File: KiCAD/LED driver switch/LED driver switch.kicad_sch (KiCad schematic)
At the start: 37 parts, among them J1 3x Banana Jack, J2 USB Jack, J3 Conn_01x04_Pin, J4 TTl-RS232, J5 JST-XH Connector, J6 8P8C_Shielded, Q1 TN2124, Q2 PMOS, SW1 Door interlock, SW2 Door interlock, SW3 Door interlock, SW4 Door interlock, U2 4.096V, U8 Itsy_Bitsy_32u4

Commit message: Initial draft
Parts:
- removed SW2, SW3: Door interlock, symbol Switch:SW_Reed
- added J7: Conn_Coaxial, Custom footprints:LINX_CONBNC001, symbol Connector:Conn_Coaxial
- added N2: Bench Supply, symbol Mechanical:Housing
- D2: footprint Custom footprints:P26_DO-214AA_SMB -> Custom footprints:SMDJSeries_LTF; Manufacturer Diotec Semiconductor -> YAGEO; Part P6SMB300A -> SMDJ220CA/TR13
- F2: Part 3403.0010.11 -> 3403.0022.24
- F3: Part 3403.0019.11 -> 3403.0022.24
- Q2: footprint Package_TO_SOT_SMD:SOT-223-3_TabPin2 -> Package_TO_SOT_SMD:TO-263-2; Part DMP45H21DHE-13 -> DMP45H4D9HK3-13
- R5: value 100 -> 1; footprint Resistor_SMD:R_1206_3216Metric -> Package_TO_SOT_SMD:TO-263-2
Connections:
- net GND: now also U8.16 (Gnd), J7.2 (Ext)
- net Isense: now also J7.1 (In)
- net Power supply+: now also F3.1; no longer F3.2
- net at D3.2 (A): now also F3.2; no longer F3.1
- net Enclosure safety interlock1: no longer names the net of U8.29 (12_A11)
- net Enclosure safety interlock2: no longer names the net of U8.28 (~11)
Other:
- moved on the sheet: J3, J4, RN2

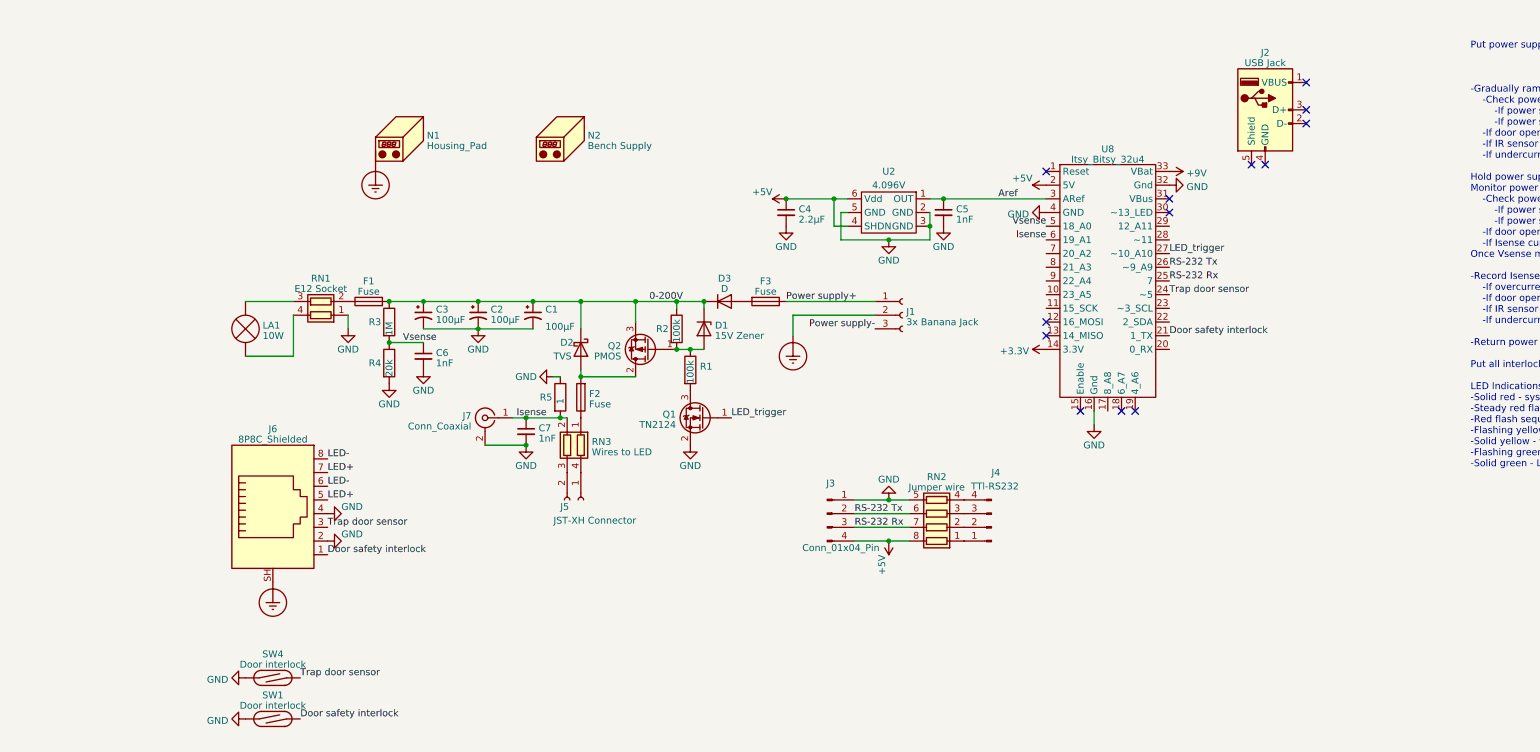
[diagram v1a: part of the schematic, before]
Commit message: Working PCB draft
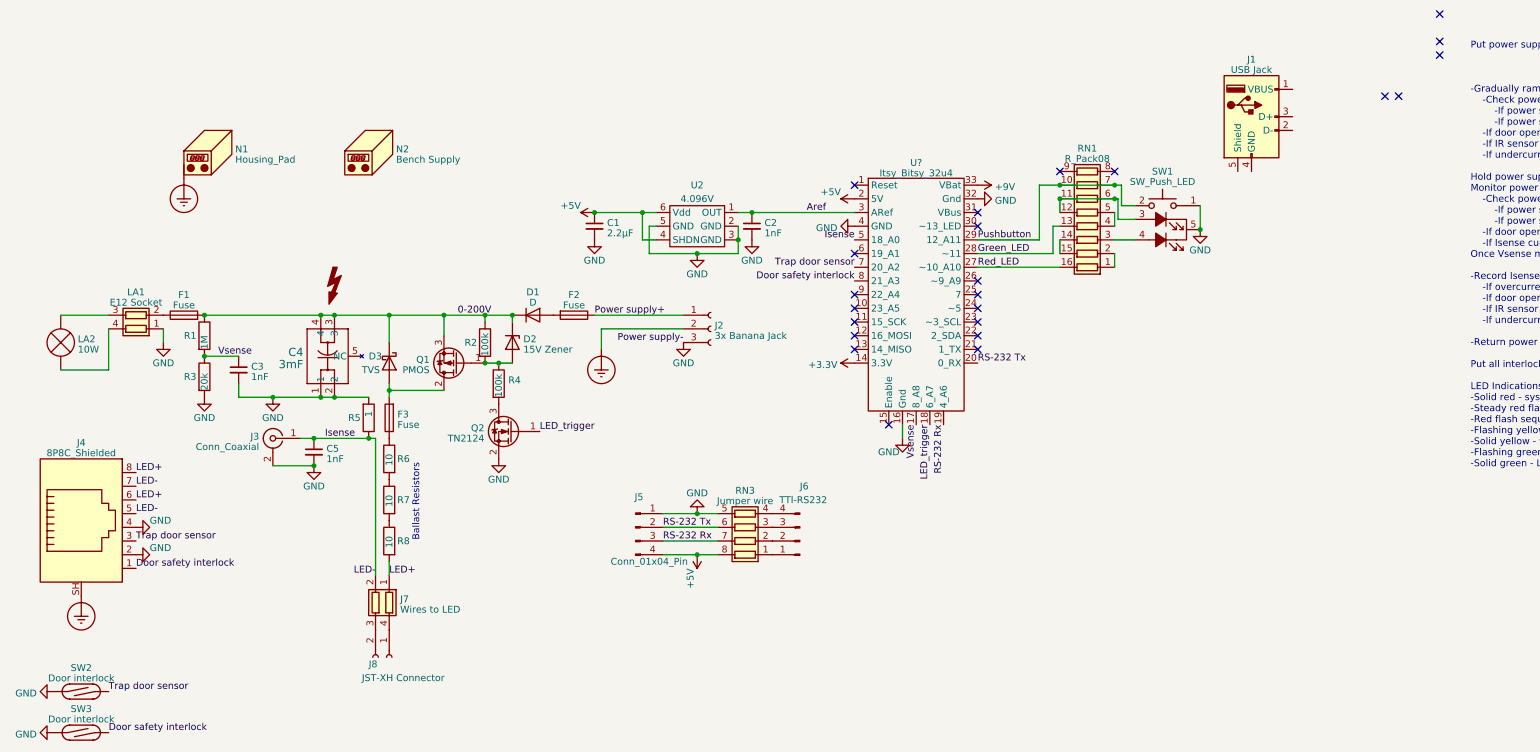
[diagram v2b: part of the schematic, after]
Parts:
- removed C1, C2, C3: 100µF, Capacitor_THT:CP_Radial_D18.0mm_P7.50mm, symbol Device:C_Polarized_Small_US
- added C4: 3mF, Custom footprints:ALF20G302KP400, symbol Custom:ALF20G223EH063
- added R6, R7, R8: 10, Package_TO_SOT_THT:TO-247-2_Vertical, symbol Device:R
- added RN1: R_Pack08, Resistor_SMD:R_Array_Convex_8x0602, symbol Device:R_Pack08
- added SW1: SW_Push_LED, Connector_Wire:SolderWire-0.1sqmm_1x05_P3.6mm_D0.4mm_OD1mm, symbol Custom:SW_Push_2x_LED_common_cathode
- added SYM1: SYM_Flash_Small, Custom footprints:Symbol_HighVoltage, symbol Graphic:SYM_Flash_Small
- J2: renamed from J1; footprint Connector_Wire:SolderWire-0.1sqmm_1x03_P3.6mm_D0.4mm_OD1mm -> Connector_Wire:SolderWire-0.15sqmm_1x03_P4mm_D0.5mm_OD1.5mm
- J3: renamed from J7; footprint Custom footprints:LINX_CONBNC001 -> Connector_Wire:SolderWire-0.1sqmm_1x02_P3.6mm_D0.4mm_OD1mm; Part CONBNC001 -> CONBNC004
- J4: renamed from J6; footprint Custom footprints:AMPHENOL_RJE3A1881402N -> Custom footprints:BEL_SS71800-019F; Manufacturer Amphenol ICC (Commercial Products) -> Stewart Connector; Part RJE3A1881402N -> SS71800-019F
- J8: renamed from J5; footprint Connector_Wire:SolderWire-0.1sqmm_1x02_P3.6mm_D0.4mm_OD1mm_Relief -> (none)
- LA1: renamed from RN1; footprint (none) -> Connector_Wire:SolderWire-0.1sqmm_1x02_P3.6mm_D0.4mm_OD1mm
- R5: footprint Package_TO_SOT_SMD:TO-263-2 -> Package_TO_SOT_THT:TO-126-2_Vertical; Manufacturer Panasonic Electronic Components -> Caddock Electronics Inc.; Part ERA-8AEB101V -> MP915-1.00-1%
- renumbered C4 to C1, C5 to C2, C6 to C3, C7 to C5, D3 to D1, D1 to D2, D2 to D3, F3 to F2, F2 to F3, J2 to J1, J3 to J5, J4 to J6, RN3 to J7, LA1 to LA2, Q2 to Q1, Q1 to Q2, R3 to R1, R4 to R3, R1 to R4, RN2 to RN3, SW4 to SW2, SW1 to SW3, U8 to U?
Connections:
- net LED- is gone; now on net LED+: J4.6, J4.8
- net Power supply- is gone; now on net GND: J2.3 (Pin_3)
- net 0-200V: now also C4.3, C4.4
- net Door safety interlock: now also U?.8 (21_A3); no longer U?.21 (1_TX)
- net GND: now also R5.2, C4.1, C4.2, SW1.1, SW1.5 (K); no longer R5.1
- net Isense: now also J4.5, J4.7, R5.1, U?.5 (18_A0); no longer R5.2, U?.6 (19_A1)
- net LED+: now also J7.1 (R1.1), R8.2; no longer J4.5, J4.7
- net LED_trigger: now also U?.18 (6_A7); no longer U?.27 (~10_A10)
- net RS-232 Rx: now also U?.19 (4_A6); no longer U?.25 (7)
- net RS-232 Tx: now also U?.20 (0_RX); no longer U?.26 (~9_A9)
- net Trap door sensor: now also U?.7 (20_A2); no longer U?.24 (~5)
- net Vsense: now also U?.17 (8_A8); no longer U?.5 (18_A0)
- net at F3.1: now also R6.1; no longer J7.1 (R1.1)
- net Green_LED: now reaches U?.28 (~11)
- net Green_LED: now also RN1.13 (R4.2)
- net Pushbutton: now reaches U?.29 (12_A11)
- net Pushbutton: now also RN1.10 (R7.2), RN1.7 (R7.1), SW1.2
- new net: R7.2, R8.1
- new net: R6.2, R7.1
- new net: RN1.1 (R1.1), RN1.2 (R2.1)
- new net: RN1.11 (R6.2), RN1.12 (R5.2), RN1.6 (R6.1), SW1.3 (A)
- new net: RN1.14 (R3.2), RN1.15 (R2.2)
- new net: RN1.3 (R3.1), SW1.4 (A)
- new net: RN1.4 (R4.1), RN1.5 (R5.1)
- new net Red_LED: RN1.16 (R1.2), U?.27 (~10_A10)
- no-connect marks 13 -> 23
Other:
- note added: "Ballast Resistors"
- moved on the sheet: C1, C2, C3, C5, D1, D2, D3, F1, F2, F3, J1, J2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

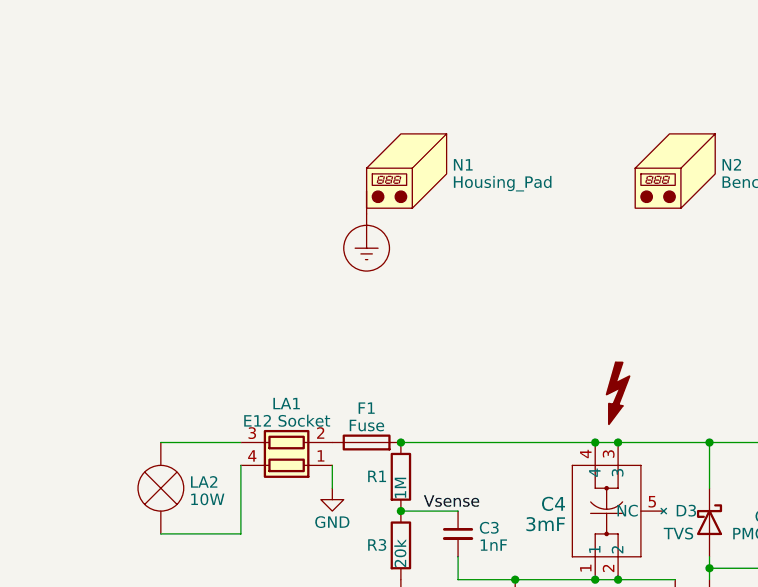
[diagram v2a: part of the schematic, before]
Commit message: standoffs and enclosure added
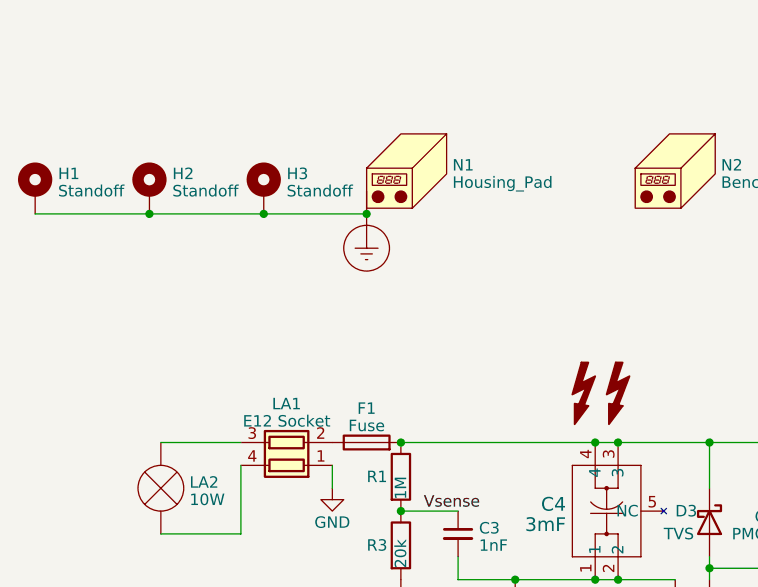
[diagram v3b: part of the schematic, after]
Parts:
- added H1, H2, H3: Standoff, Custom footprints:8-32 Standoff, symbol Mechanical:MountingHole_Pad
- added SYM2: SYM_Flash_Small, Symbol:Symbol_Highvoltage_Type2_CopperTop_Small, symbol Graphic:SYM_Flash_Small
- N1: Manufacturer (none) -> Bud Industries; Part (none) -> CU-3007-A
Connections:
- net Earth_Protective: now also H1.1, H2.1, H3.1
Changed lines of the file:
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@@
   (junction (at 259.715 46.355) (diameter 0) (color 0 0 0 0)
   )
+  (junction (at 46.99 36.83) (diameter 0) (color 0 0 0 0)
+  )
   (junction (at 87.63 77.47) (diameter 0) (color 0 0 0 0)
   )
@@
   (junction (at 129.54 71.12) (diameter 0) (color 0 0 0 0)
   )
+  (junction (at 59.69 36.83) (diameter 0) (color 0 0 0 0)
+  )
   (junction (at 243.84 38.1) (diameter 0) (color 0 0 0 0)
   )
@@
   )
   (junction (at 105.41 85.09) (diameter 0) (color 0 0 0 0)
+  )
+  (junction (at 71.12 36.83) (diameter 0) (color 0 0 0 0)
   )
   (no_connect (at 218.44 63.5))
@@
     (stroke (width 0) (type default))
   )
+  (wire (pts (xy 59.69 36.83) (xy 71.12 36.83))
+    (stroke (width 0) (type default))
+  )
   (wire (pts (xy 127 71.12) (xy 129.54 71.12))
     (stroke (width 0) (type default))
@@
     (stroke (width 0) (type default))
   )
+  (wire (pts (xy 34.29 36.83) (xy 46.99 36.83))
+    (stroke (width 0) (type default))
+  )
   (wire (pts (xy 232.41 50.8) (xy 232.41 45.72))
     (stroke (width 0) (type default))
@@
   )
   (wire (pts (xy 99.06 77.47) (xy 105.41 77.47))
+    (stroke (width 0) (type default))
+  )
+  (wire (pts (xy 46.99 36.83) (xy 59.69 36.83))
     (stroke (width 0) (type default))
   )
@@
         (path "/81d2b430-cb23-414b-8bc0-910fdb221d10"
           (reference "R7") (unit 1)
+        )
+      )
+    )
+  )
+  (symbol (lib_id "Mechanical:MountingHole_Pad") (at 34.29 34.29 0) (unit 1)
+    (in_bom yes) (on_board yes) (dnp no) (fields_autoplaced)
+    (property "Reference" "H1" (at 36.83 32.3763 0)
+      (effects (font (size 1.27 1.27)) (justify left))
+    )
+    (property "Value" "Standoff" (at 36.83 34.2973 0)
+      (effects (font (size 1.27 1.27)) (justify left))
+    )
+    (property "Footprint" "Custom footprints:8-32 Standoff" (at 34.29 34.29 0)
+      (effects (font (size 1.27 1.27)) hide)
+    )
+    (property "Datasheet" "http://dpk3n3gg92jwt.cloudfront.net/domains/raf/pdf/RAF_catalog_0122.pdf" (at 34.29 34.29 0)
+      (effects (font (size 1.27 1.27)) hide)
+    )
+    (property "Manufacturer" "RAF Electronic Hardware" (at 34.29 34.29 0)
+      (effects (font (size 1.27 1.27)) hide)
+    )
+    (property "Part" "4534-832-AL-7" (at 34.29 34.29 0)
+      (effects (font (size 1.27 1.27)) hide)
+    )
+    (pin "1")
+    (instances
+      (project "LED driver switch"
+        (path "/81d2b430-cb23-414b-8bc0-910fdb221d10"
+          (reference "H1") (unit 1)
         )
       )
@@
         (path "/f63253f1-d78d-4fac-a266-90df8fae5286"
           (reference "#PWR?") (unit 1)
+        )
+      )
+    )
+  )
+  (symbol (lib_id "Mechanical:MountingHole_Pad") (at 59.69 34.29 0) (unit 1)
+    (in_bom yes) (on_board yes) (dnp no) (fields_autoplaced)
+    (property "Reference" "H3" (at 62.23 32.3763 0)
+      (effects (font (size 1.27 1.27)) (justify left))
+    )
+    (property "Value" "Standoff" (at 62.23 34.2973 0)
+      (effects (font (size 1.27 1.27)) (justify left))
+    )
+    (property "Footprint" "Custom footprints:8-32 Standoff" (at 59.69 34.29 0)
+      (effects (font (size 1.27 1.27)) hide)
+    )
+    (property "Datasheet" "http://dpk3n3gg92jwt.cloudfront.net/domains/raf/pdf/RAF_catalog_0122.pdf" (at 59.69 34.29 0)
+      (effects (font (size 1.27 1.27)) hide)
+    )
+    (property "Manufacturer" "RAF Electronic Hardware" (at 59.69 34.29 0)
+      (effects (font (size 1.27 1.27)) hide)
+    )
+    (property "Part" "4534-832-AL-7" (at 59.69 34.29 0)
+      (effects (font (size 1.27 1.27)) hide)
+    )
+    (pin "1")
+    (instances
+      (project "LED driver switch"
+        (path "/81d2b430-cb23-414b-8bc0-910fdb221d10"
+          (reference "H3") (unit 1)
         )
       )
@@
     )
   )
+  (symbol (lib_id "Mechanical:MountingHole_Pad") (at 46.99 34.29 0) (unit 1)
+    (in_bom yes) (on_board yes) (dnp no) (fields_autoplaced)
+    (property "Reference" "H2" (at 49.53 32.3763 0)
+      (effects (font (size 1.27 1.27)) (justify left))
+    )
+    (property "Value" "Standoff" (at 49.53 34.2973 0)
+      (effects (font (size 1.27 1.27)) (justify left))
+    )
+    (property "Footprint" "Custom footprints:8-32 Standoff" (at 46.99 34.29 0)
+      (effects (font (size 1.27 1.27)) hide)
+    )
+    (property "Datasheet" "http://dpk3n3gg92jwt.cloudfront.net/domains/raf/pdf/RAF_catalog_0122.pdf" (at 46.99 34.29 0)
+      (effects (font (size 1.27 1.27)) hide)
+    )
+    (property "Manufacturer" "RAF Electronic Hardware" (at 46.99 34.29 0)
+      (effects (font (size 1.27 1.27)) hide)
+    )
+    (property "Part" "4534-832-AL-7" (at 46.99 34.29 0)
+      (effects (font (size 1.27 1.27)) hide)
+    )
+    (pin "1")
+    (instances
+      (project "LED driver switch"
+        (path "/81d2b430-cb23-414b-8bc0-910fdb221d10"
+          (reference "H2") (unit 1)
+        )
+      )
+    )
+  )
   (symbol (lib_id "Device:D_Schottky") (at 109.22 71.12 270) (unit 1)
     (in_bom yes) (on_board yes) (dnp no)
@@
     )
   )
+  (symbol (lib_id "Graphic:SYM_Flash_Small") (at 95.25 57.15 0) (unit 1)
+    (in_bom no) (on_board yes) (dnp no) (fields_autoplaced)
+    (property "Reference" "SYM2" (at 92.964 57.15 90)
+      (effects (font (size 1.27 1.27)) hide)
+    )
+    (property "Value" "SYM_Flash_Small" (at 97.536 57.15 90)
+      (effects (font (size 1.27 1.27)) hide)
+    )
+    (property "Footprint" "Symbol:Symbol_Highvoltage_Type2_CopperTop_Small" (at 95.25 57.785 0)
+      (effects (font (size 1.27 1.27)) hide)
+    )
+    (property "Datasheet" "~" (at 105.41 59.69 0)
+      (effects (font (size 1.27 1.27)) hide)
+    )
+    (property "Sim.Enable" "0" (at 95.25 57.15 0)
+      (effects (font (size 1.27 1.27)) hide)
+    )
+    (property "Manufacturer" "" (at 95.25 57.15 0)
+      (effects (font (size 1.27 1.27)) hide)
+    )
+    (property "Part" "" (at 95.25 57.15 0)
+      (effects (font (size 1.27 1.27)) hide)
+    )
+    (instances
+      (project "LED driver switch"
+        (path "/81d2b430-cb23-414b-8bc0-910fdb221d10"
+          (reference "SYM2") (unit 1)
+        )
+      )
+    )
+  )
   (symbol (lib_id "Connector:Conn_01x04_Pin") (at 154.94 101.6 0) (unit 1)
     (in_bom yes) (on_board yes) (dnp no)
@@
       (effects (font (size 1.27 1.27)) hide)
     )
-    (property "Datasheet" "~" (at 78.105 30.48 0)
-      (effects (font (size 1.27 1.27)) hide)
-    )
-    (property "Manufacturer" "" (at 76.2 31.75 0)
-      (effects (font (size 1.27 1.27)) hide)
-    )
-    (property "Part" "" (at 76.2 31.75 0)
-      (effects (font (size 1.27 1.27)) hide)
-    )
+    (property "Datasheet" "https://www.budind.com/wp-content/uploads/2019/01/hb2100b-1.pdf" (at 78.105 30.48 0)
+      (effects (font (size 1.27 1.27)) hide)
+    )
+    (property "Manufacturer" "Bud Industries" (at 76.2 31.75 0)
+      (effects (font (size 1.27 1.27)) hide)
+    )
+    (property "Part" "CU-3007-A" (at 76.2 31.75 0)
+      (effects (font (size 1.27 1.27)) hide)
+    )

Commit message: Add pulldown to gate, move LED pin to PWM
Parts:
- added R9: 20k, Resistor_SMD:R_0603_1608Metric, symbol Device:R
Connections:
- net GND: now also R9.2
- net LED_trigger: now also U?.23 (~3_SCL), R9.1; no longer U?.18 (6_A7)
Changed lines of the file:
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@@
   (junction (at 71.12 36.83) (diameter 0) (color 0 0 0 0)
   )
-  (no_connect (at 218.44 63.5))
+  (no_connect (at 209.55 82.55))
   (no_connect (at 195.58 58.42))
   (no_connect (at 304.165 6.35))
@@
     (effects (font (size 1.27 1.27)) (justify left bottom))
   )
-  (label "LED_trigger" (at 209.55 82.55 270) (fields_autoplaced)
-    (effects (font (size 1.27 1.27)) (justify right bottom))
+  (label "LED_trigger" (at 218.44 63.5 0) (fields_autoplaced)
+    (effects (font (size 1.27 1.27)) (justify left bottom))
   )
   (label "Door safety interlock" (at 62.23 109.22 0) (fields_autoplaced)
@@
     )
   )
+  (symbol (lib_id "Device:R") (at 137.16 87.63 0) (unit 1)
+    (in_bom yes) (on_board yes) (dnp no)
+    (property "Reference" "R9" (at 133.35 87.63 0)
+      (effects (font (size 1.27 1.27)) (justify left))
+    )
+    (property "Value" "20k" (at 137.16 90.17 90)
+      (effects (font (size 1.27 1.27)) (justify left))
+    )
+    (property "Footprint" "Resistor_SMD:R_0603_1608Metric" (at 135.382 87.63 90)
+      (effects (font (size 1.27 1.27)) hide)
+    )
+    (property "Datasheet" "https://industrial.panasonic.com/cdbs/www-data/pdf/RDM0000/AOA0000C307.pdf" (at 137.16 87.63 0)
+      (effects (font (size 1.27 1.27)) hide)
+    )
+    (property "Manufacturer" "Panasonic Electronic Components" (at 137.16 87.63 0)
+      (effects (font (size 1.27 1.27)) hide)
+    )
+    (property "Part" "ERA-3AEB203V" (at 137.16 87.63 0)
+      (effects (font (size 1.27 1.27)) hide)
+    )
+    (pin "1")
+    (pin "2")
+    (instances
+      (project "LED driver switch"
+        (path "/81d2b430-cb23-414b-8bc0-910fdb221d10"
+          (reference "R9") (unit 1)
+        )
+      )
+    )
+  )
   (symbol (lib_id "Device:Lamp") (at 48.26 67.31 180) (unit 1)
     (in_bom yes) (on_board no) (dnp no) (fields_autoplaced)
@@
         )
       )
+      (project "Dual encoder controller"
+        (path "/f63253f1-d78d-4fac-a266-90df8fae5286"
+          (reference "#PWR?") (unit 1)
+        )
+      )
+    )
+  )
+  (symbol (lib_id "power:GND") (at 137.16 91.44 0) (unit 1)
+    (in_bom yes) (on_board yes) (dnp no)
+    (property "Reference" "#PWR027" (at 137.16 97.79 0)
+      (effects (font (size 1.27 1.27)) hide)
+    )
+    (property "Value" "GND" (at 137.16 95.25 0)
+      (effects (font (size 1.27 1.27)))
+    )
+    (property "Footprint" "" (at 137.16 91.44 0)
+      (effects (font (size 1.27 1.27)) hide)
+    )
+    (property "Datasheet" "" (at 137.16 91.44 0)
+      (effects (font (size 1.27 1.27)) hide)
+    )
+    (pin "1")
+    (instances
+      (project "LED driver switch"
+        (path "/81d2b430-cb23-414b-8bc0-910fdb221d10"
+          (reference "#PWR027") (unit 1)
+        )
+      )
